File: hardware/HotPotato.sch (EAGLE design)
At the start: 13 parts, among them M1 SANYO_NRS-2574SMT, SW1 TACTILE-SWITCH-PTH, U1 TINY85-20-DIP

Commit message: Change LED package to 5mm
Fixes #2
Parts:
- D3: device SparkFun-LED:LED1206 -> SparkFun-LED:LED5MM-KIT
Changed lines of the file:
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@@
 <grid distance="0.1" unitdist="inch" unit="inch" style="lines" multiple="1" display="no" altdistance="0.01" altunitdist="inch" altunit="inch"/>
 <layers>
-<layer number="1" name="Top" color="4" fill="1" visible="no" active="no"/>
-<layer number="2" name="Route2" color="1" fill="3" visible="no" active="no"/>
-<layer number="3" name="Route3" color="4" fill="3" visible="no" active="no"/>
-<layer number="4" name="Route4" color="1" fill="4" visible="no" active="no"/>
-<layer number="5" name="Route5" color="4" fill="4" visible="no" active="no"/>
-<layer number="6" name="Route6" color="1" fill="8" visible="no" active="no"/>
-<layer number="7" name="Route7" color="4" fill="8" visible="no" active="no"/>
-<layer number="8" name="Route8" color="1" fill="2" visible="no" active="no"/>
-<layer number="9" name="Route9" color="4" fill="2" visible="no" active="no"/>
-<layer number="10" name="Route10" color="1" fill="7" visible="no" active="no"/>
-<layer number="11" name="Route11" color="4" fill="7" visible="no" active="no"/>
-<layer number="12" name="Route12" color="1" fill="5" visible="no" active="no"/>
-<layer number="13" name="Route13" color="4" fill="5" visible="no" active="no"/>
-<layer number="14" name="Route14" color="1" fill="6" visible="no" active="no"/>
-<layer number="15" name="Route15" color="4" fill="6" visible="no" active="no"/>
-<layer number="16" name="Bottom" color="1" fill="1" visible="no" active="no"/>
-<layer number="17" name="Pads" color="2" fill="1" visible="no" active="no"/>
-<layer number="18" name="Vias" color="2" fill="1" visible="no" active="no"/>
-<layer number="19" name="Unrouted" color="6" fill="1" visible="no" active="no"/>
-<layer number="20" name="Dimension" color="15" fill="1" visible="no" active="no"/>
-<layer number="21" name="tPlace" color="7" fill="1" visible="no" active="no"/>
-<layer number="22" name="bPlace" color="7" fill="1" visible="no" active="no"/>
-<layer number="23" name="tOrigins" color="15" fill="1" visible="no" active="no"/>
-<layer number="24" name="bOrigins" color="15" fill="1" visible="no" active="no"/>
-<layer number="25" name="tNames" color="7" fill="1" visible="no" active="no"/>
-<layer number="26" name="bNames" color="7" fill="1" visible="no" active="no"/>
-<layer number="27" name="tValues" color="7" fill="1" visible="no" active="no"/>
-<layer number="28" name="bValues" color="7" fill="1" visible="no" active="no"/>
+<layer number="1" name="Top" color="4" fill="1" visible="yes" active="no"/>
+<layer number="2" name="Route2" color="1" fill="3" visible="yes" active="no"/>
+<layer number="3" name="Route3" color="4" fill="3" visible="yes" active="no"/>
+<layer number="4" name="Route4" color="1" fill="4" visible="yes" active="no"/>
+<layer number="5" name="Route5" color="4" fill="4" visible="yes" active="no"/>
+<layer number="6" name="Route6" color="1" fill="8" visible="yes" active="no"/>
+<layer number="7" name="Route7" color="4" fill="8" visible="yes" active="no"/>
+<layer number="8" name="Route8" color="1" fill="2" visible="yes" active="no"/>
+<layer number="9" name="Route9" color="4" fill="2" visible="yes" active="no"/>
+<layer number="10" name="Route10" color="1" fill="7" visible="yes" active="no"/>
+<layer number="11" name="Route11" color="4" fill="7" visible="yes" active="no"/>
+<layer number="12" name="Route12" color="1" fill="5" visible="yes" active="no"/>
+<layer number="13" name="Route13" color="4" fill="5" visible="yes" active="no"/>
+<layer number="14" name="Route14" color="1" fill="6" visible="yes" active="no"/>
+<layer number="15" name="Route15" color="4" fill="6" visible="yes" active="no"/>
+<layer number="16" name="Bottom" color="1" fill="1" visible="yes" active="no"/>
+<layer number="17" name="Pads" color="2" fill="1" visible="yes" active="no"/>
+<layer number="18" name="Vias" color="2" fill="1" visible="yes" active="no"/>
+<layer number="19" name="Unrouted" color="6" fill="1" visible="yes" active="no"/>
+<layer number="20" name="Dimension" color="15" fill="1" visible="yes" active="no"/>
+<layer number="21" name="tPlace" color="7" fill="1" visible="yes" active="no"/>
+<layer number="22" name="bPlace" color="7" fill="1" visible="yes" active="no"/>
+<layer number="23" name="tOrigins" color="15" fill="1" visible="yes" active="no"/>
+<layer number="24" name="bOrigins" color="15" fill="1" visible="yes" active="no"/>
+<layer number="25" name="tNames" color="7" fill="1" visible="yes" active="no"/>
+<layer number="26" name="bNames" color="7" fill="1" visible="yes" active="no"/>
+<layer number="27" name="tValues" color="7" fill="1" visible="yes" active="no"/>
+<layer number="28" name="bValues" color="7" fill="1" visible="yes" active="no"/>
 <layer number="29" name="tStop" color="7" fill="3" visible="no" active="no"/>
 <layer number="30" name="bStop" color="7" fill="6" visible="no" active="no"/>
@@
 <layer number="35" name="tGlue" color="7" fill="4" visible="no" active="no"/>
 <layer number="36" name="bGlue" color="7" fill="5" visible="no" active="no"/>
-<layer number="37" name="tTest" color="7" fill="1" visible="no" active="no"/>
-<layer number="38" name="bTest" color="7" fill="1" visible="no" active="no"/>
+<layer number="37" name="tTest" color="7" fill="1" visible="yes" active="no"/>
+<layer number="38" name="bTest" color="7" fill="1" visible="yes" active="no"/>
 <layer number="39" name="tKeepout" color="4" fill="11" visible="no" active="no"/>
 <layer number="40" name="bKeepout" color="1" fill="11" visible="no" active="no"/>
@@
 <layer number="44" name="Drills" color="7" fill="1" visible="no" active="no"/>
 <layer number="45" name="Holes" color="7" fill="1" visible="no" active="no"/>
-<layer number="46" name="Milling" color="3" fill="1" visible="no" active="no"/>
-<layer number="47" name="Measures" color="7" fill="1" visible="no" active="no"/>
-<layer number="48" name="Document" color="7" fill="1" visible="no" active="no"/>
-<layer number="49" name="Reference" color="7" fill="1" visible="no" active="no"/>
-<layer number="50" name="dxf" color="7" fill="1" visible="no" active="no"/>
-<layer number="51" name="tDocu" color="7" fill="1" visible="no" active="no"/>
-<layer number="52" name="bDocu" color="7" fill="1" visible="no" active="no"/>
-<layer number="53" name="tGND_GNDA" color="7" fill="9" visible="no" active="no"/>
-<layer number="54" name="bGND_GNDA" color="1" fill="9" visible="no" active="no"/>
-<layer number="56" name="wert" color="7" fill="1" visible="no" active="no"/>
-<layer number="57" name="tCAD" color="7" fill="1" visible="no" active="no"/>
-<layer number="59" name="tCarbon" color="7" fill="1" visible="no" active="no"/>
-<layer number="60" name="bCarbon" color="7" fill="1" visible="no" active="no"/>
+<layer number="46" name="Milling" color="3" fill="1" visible="yes" active="no"/>
+<layer number="47" name="Measures" color="7" fill="1" visible="yes" active="no"/>
+<layer number="48" name="Document" color="7" fill="1" visible="yes" active="no"/>
+<layer number="49" name="Reference" color="7" fill="1" visible="yes" active="no"/>
+<layer number="50" name="dxf" color="7" fill="1" visible="yes" active="no"/>
+<layer number="51" name="tDocu" color="7" fill="1" visible="yes" active="no"/>
+<layer number="52" name="bDocu" color="7" fill="1" visible="yes" active="no"/>
+<layer number="53" name="tGND_GNDA" color="7" fill="9" visible="yes" active="no"/>
+<layer number="54" name="bGND_GNDA" color="1" fill="9" visible="yes" active="no"/>
+<layer number="56" name="wert" color="7" fill="1" visible="yes" active="no"/>
+<layer number="57" name="tCAD" color="7" fill="1" visible="yes" active="no"/>
+<layer number="59" name="tCarbon" color="7" fill="1" visible="yes" active="no"/>
+<layer number="60" name="bCarbon" color="7" fill="1" visible="yes" active="no"/>
 <layer number="90" name="Modules" color="5" fill="1" visible="yes" active="yes"/>
 <layer number="91" name="Nets" color="2" fill="1" visible="yes" active="yes"/>
@@
 <part name="U1" library="SparkFun-DigitalIC" deviceset="ATTINY45" device="TINY85-20-DIP" value="TINY85-20-DIP"/>
 <part name="R2" library="SparkFun-Passives" deviceset="RESISTOR" device="1206" value="220Ω"/>
-<part name="D3" library="SparkFun-LED" deviceset="LED" device="1206"/>
+<part name="D3" library="SparkFun-LED" deviceset="LED" device="5MM-KIT"/>
 <part name="BATTERY_1" library="Itead_BP_110825.lbr" deviceset="BATTERY_1236_C" device=""/>
 <part name="SW1" library="GeekAmmo" deviceset="TACTILE-SWITCH" device="-PTH"/>

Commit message: Add reset button
Fixes #1
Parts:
- added K1: TS-1101F, Seeed-OPL-Button:DIP-BUTTON-FRONT-WHITE(2P-3.4X6MM)
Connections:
- removed net RST: R5.1, U1.PB5(NRES)
- new net N$6: K1.1, R5.1, U1.PB5(NRES)
- net GND: now also K1.2
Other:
- moved on the sheet: R5

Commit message: Increase distance between buzzer poles
Fixes #4
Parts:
- removed SG2: BUZZER, dhgoldberg:BUZZER
- added SG1: BUZZER9MM, dhgoldberg:BUZZER9MM
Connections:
- net BUZZ: now also SG1.1; no longer SG2.1
- net N$5: now also SG1.2; no longer SG2.2

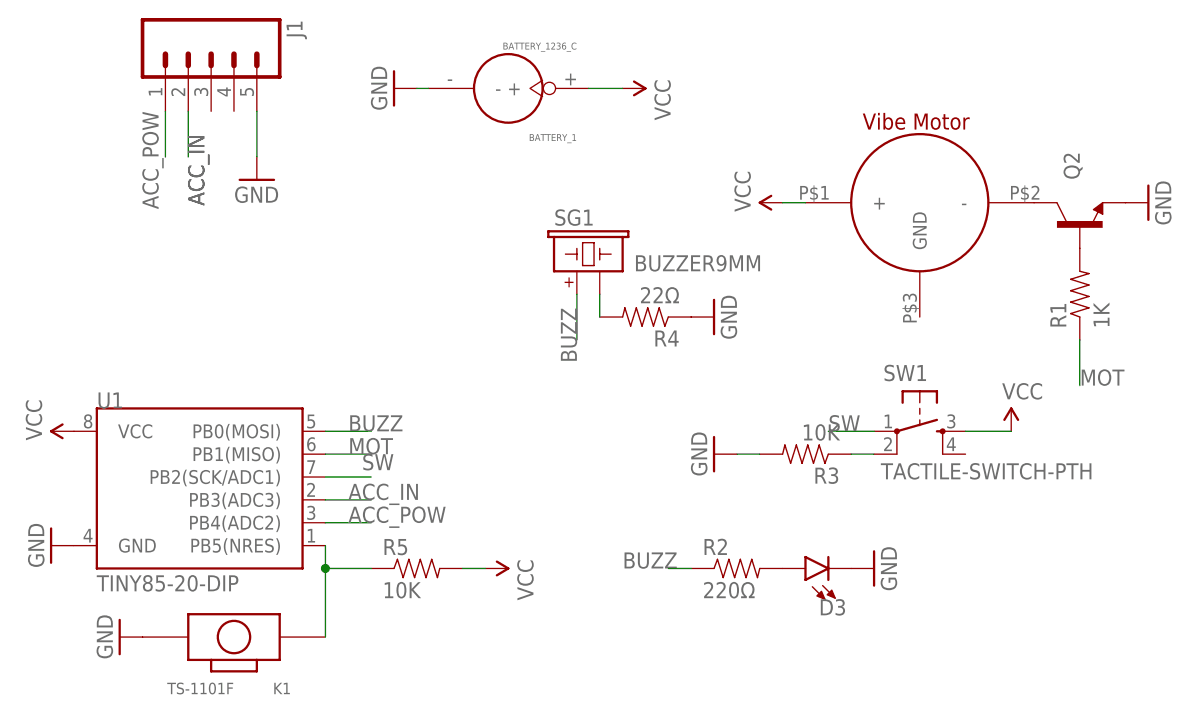
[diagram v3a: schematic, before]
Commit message: Remove accelerometer header and set dedicated LED pin
[hw rev. 3]
Since the Hot Potato (game) use case was deemed less significant
hardware support for it was removed in order to leave more space
for the common components. This also enabled us to use a dedicated
pin for the LED which was previously routed in parallel with the
buzzer.  This should enable better control over the hardware and
(theoretically) more current to be supplied to the LED and the
buzzer.
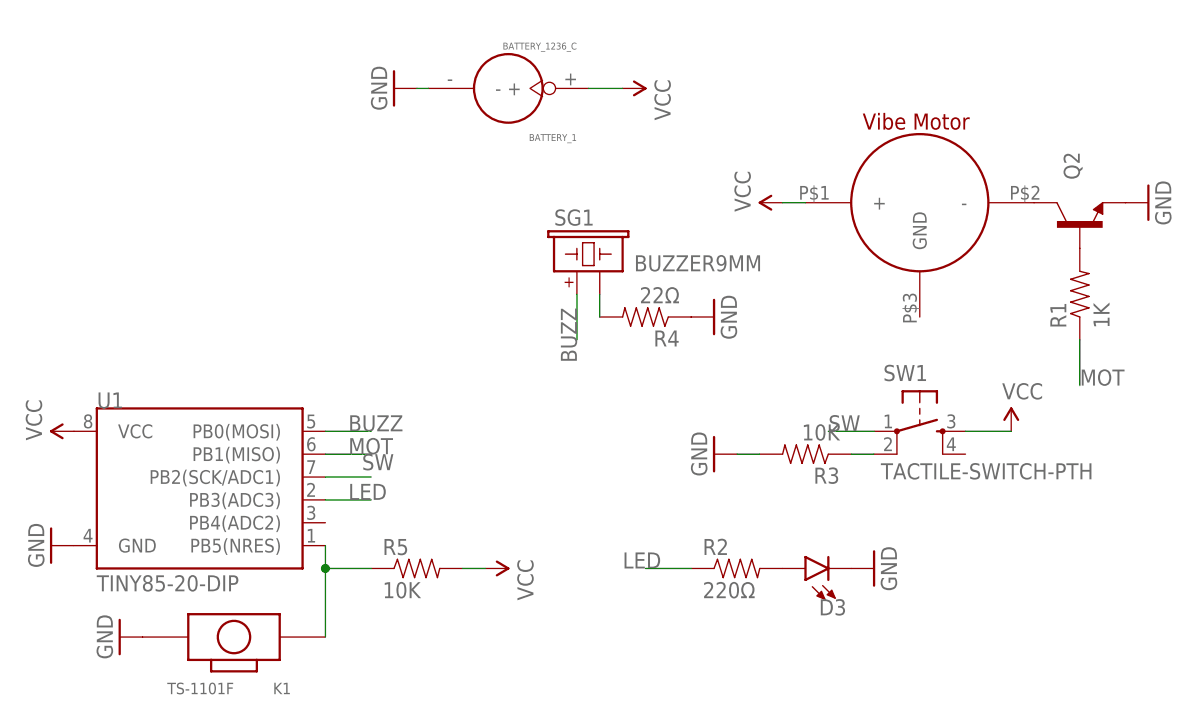
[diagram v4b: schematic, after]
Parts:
- removed J1: (no value), SparkFun-Connectors:M05PTH
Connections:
- removed net ACC_IN: J1.2, U1.PB3(ADC3)
- removed net ACC_POW: J1.1, U1.PB4(ADC2)
- new net LED: R2.1, U1.PB3(ADC3)
- net BUZZ: no longer R2.1
- net GND: no longer J1.5
